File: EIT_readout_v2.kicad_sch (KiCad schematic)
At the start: 16 parts, among them J4 Conn_Coaxial_Small, J5 Conn_Coaxial_Small, J6 Conn_Coaxial_Small, U1 Teensy4.0, U2 MAX336CWI+, U3 MAX336CWI+, U4 LTC1983ES6-3-TRPBF

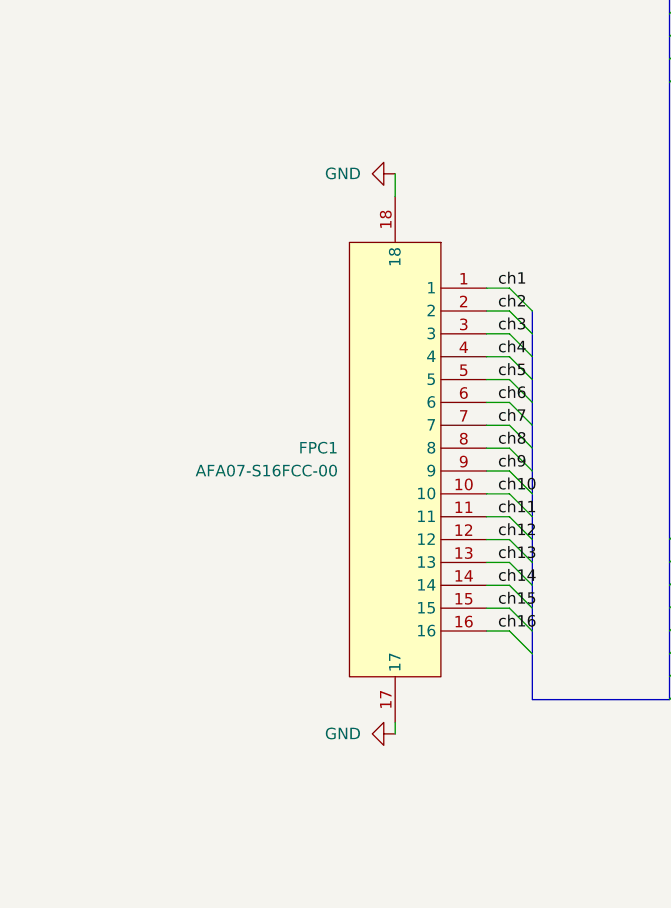
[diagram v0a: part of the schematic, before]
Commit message: changed the readout PCB FPC holder to 18 pins to accommodate ground
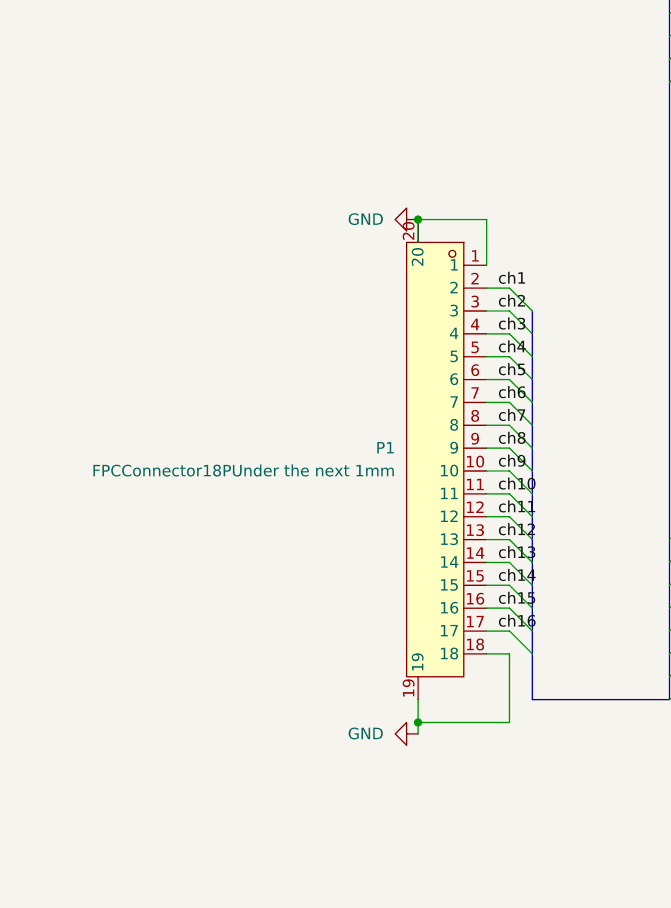
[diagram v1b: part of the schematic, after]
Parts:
- removed FPC1: AFA07-S16FCC-00, easyeda2kicad:FPC-SMD_16P-P1.00_AFA07-S16FCC-00, symbol easyeda2kicad:AFA07-S16FCC-00
- added P1: FPCConnector18PUnder the next 1mm, easyeda2kicad:FPC-SMD_18P-P1.00_AFA07-S18FCC-00, symbol easyeda2kicad:FPCConnector18PUnderthenext1mm
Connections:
- net GND: now also P1.1, P1.18, P1.19, P1.20
- net ch1: now also P1.2
- net ch10: now also P1.11
- net ch11: now also P1.12
- net ch12: now also P1.13
- net ch13: now also P1.14
- net ch14: now also P1.15
- net ch15: now also P1.16
- net ch16: now also P1.17
- net ch2: now also P1.3
- net ch3: now also P1.4
- net ch4: now also P1.5
- net ch5: now also P1.6
- net ch6: now also P1.7
- net ch7: now also P1.8
- net ch8: now also P1.9
- net ch9: now also P1.10
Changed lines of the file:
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@@
 		(color 0 0 0 0)
 	)
+	(junction
+		(at 45.72 139.7)
+		(diameter 0)
+		(color 0 0 0 0)
+	)
+	(junction
+		(at 45.72 83.82)
+		(diameter 0)
+		(color 0 0 0 0)
+	)
 	(no_connect
 		(at 198.12 45.72)
@@
 	(wire
 		(pts
-			(xy 43.18 78.74) (xy 43.18 81.28)
+			(xy 45.72 83.82) (xy 45.72 86.36)
 		)
 		(stroke
@@
 	(wire
 		(pts
+			(xy 55.88 132.08) (xy 55.88 139.7)
+		)
+		(stroke
+			(width 0)
+			(type default)
+		)
+	)
+	(wire
+		(pts
 			(xy 193.04 142.24) (xy 204.47 142.24)
 		)
@@
 	(wire
 		(pts
+			(xy 53.34 83.82) (xy 45.72 83.82)
+		)
+		(stroke
+			(width 0)
+			(type default)
+		)
+	)
+	(wire
+		(pts
 			(xy 85.09 95.25) (xy 85.09 97.79)
 		)
@@
 	(wire
 		(pts
+			(xy 53.34 132.08) (xy 55.88 132.08)
+		)
+		(stroke
+			(width 0)
+			(type default)
+		)
+	)
+	(wire
+		(pts
 			(xy 76.2 129.54) (xy 86.36 129.54)
 		)
@@
 	(wire
 		(pts
-			(xy 43.18 139.7) (xy 43.18 140.97)
+			(xy 45.72 139.7) (xy 45.72 140.97)
 		)
 		(stroke
@@
 	(wire
 		(pts
+			(xy 53.34 88.9) (xy 53.34 83.82)
+		)
+		(stroke
+			(width 0)
+			(type default)
+		)
+	)
+	(wire
+		(pts
 			(xy 53.34 129.54) (xy 55.88 129.54)
 		)
@@
 	(wire
 		(pts
+			(xy 55.88 139.7) (xy 45.72 139.7)
+		)
+		(stroke
+			(width 0)
+			(type default)
+		)
+	)
+	(wire
+		(pts
 			(xy 76.2 53.34) (xy 86.36 53.34)
 		)
@@
 		)
 	)
+	(wire
+		(pts
+			(xy 45.72 137.16) (xy 45.72 139.7)
+		)
+		(stroke
+			(width 0)
+			(type default)
+		)
+	)
 	(bus
 		(pts
@@
 	(symbol
 		(lib_id "power:GND")
-		(at 43.18 78.74 270)
+		(at 45.72 83.82 270)
 		(unit 1)
 		(exclude_from_sim no)
@@
 		(fields_autoplaced yes)
 		(property "Reference" "#PWR020"
-			(at 36.83 78.74 0)
+			(at 39.37 83.82 0)
 			(effects
 				(font
@@
 		)
 		(property "Value" "GND"
-			(at 39.37 78.7399 90)
+			(at 41.91 83.8199 90)
 			(effects
 				(font
@@
 		)
 		(property "Footprint" ""
-			(at 43.18 78.74 0)
+			(at 45.72 83.82 0)
 			(effects
 				(font
@@
 		)
 		(property "Datasheet" ""
-			(at 43.18 78.74 0)
+			(at 45.72 83.82 0)
 			(effects
 				(font
@@
 		)
 		(property "Description" "Power symbol creates a global label with name \"GND\" , ground"
-			(at 43.18 78.74 0)
+			(at 45.72 83.82 0)
 			(effects
 				(font
@@
 	)
 	(symbol
+		(lib_id "easyeda2kicad:FPCConnector18PUnderthenext1mm")
+		(at 49.53 110.49 0)
+		(mirror y)
+		(unit 1)
+		(exclude_from_sim no)
+		(in_bom yes)
+		(on_board yes)
+		(dnp no)
+		(property "Reference" "P1"
+			(at 43.18 109.2199 0)
+			(effects
+				(font
+					(size 1.27 1.27)
+				)
+				(justify left)
+			)
+		)
+		(property "Value" "FPCConnector18PUnder the next 1mm"
+			(at 43.18 111.7599 0)
+			(effects
+				(font
+					(size 1.27 1.27)
+				)
+				(justify left)
+			)
+		)
+		(property "Footprint" "easyeda2kicad:FPC-SMD_18P-P1.00_AFA07-S18FCC-00"
+			(at 49.53 144.78 0)
+			(effects
+				(font
+					(size 1.27 1.27)
+				)
+				(hide yes)
+			)
+		)
+		(property "Datasheet" "https://lcsc.com/product-detail/FPC-Connectors_FPC-1-0mmpitch-18P-Pull-type-Under-the-next_C23826.html"
+			(at 49.53 147.32 0)
+			(effects
+				(font
+					(size 1.27 1.27)
+				)
+				(hide yes)
+			)
+		)
+		(property "Description" "FPC 1.0mm 18P"
+			(at 49.53 110.49 0)
+			(effects
+				(font
+					(size 1.27 1.27)
+				)
+				(hide yes)
+			)
+		)
+		(property "Manufacturer" "JS(钜硕电子)"
+			(at 49.53 149.86 0)
+			(effects
+				(font
+					(size 1.27 1.27)
+				)
+				(hide yes)
+			)
+		)
+		(property "MPN" "AFA07-S18FCC-00"
+			(at 49.53 152.4 0)
+			(effects
+				(font
+					(size 1.27 1.27)
+				)
+				(hide yes)
+			)
+		)
+		(property "LCSC Part" "C23826"
+			(at 49.53 154.94 0)
+			(effects
+				(font
+					(size 1.27 1.27)
+				)
+				(hide yes)
+			)
+		)
+		(pin "7"
+		)
+		(pin "4"
+		)
+		(pin "13"
+		)
+		(pin "2"
+		)
+		(pin "5"
+		)
+		(pin "16"
+		)
+		(pin "20"
+		)
+		(pin "3"
+		)
+		(pin "6"
+		)
+		(pin "9"
+		)
+		(pin "10"
+		)
+		(pin "15"
+		)
+		(pin "11"
+		)
+		(pin "19"
+		)
+		(pin "18"
+		)
+		(pin "1"
+		)
+		(pin "8"
+		)
+		(pin "14"
+		)
+		(pin "17"
+		)
+		(pin "12"
+		)
+		(instances
+			(project ""
+				(path "/e5542335-9a9c-475b-927f-3f88279fb344"
+					(reference "P1")
+					(unit 1)
+				)
+			)
+		)
+	)
+	(symbol
 		(lib_id "power:GND")
 		(at 278.13 85.09 180)
@@
 	(symbol
 		(lib_id "power:GND")
-		(at 43.18 140.97 270)
+		(at 45.72 140.97 270)
 		(unit 1)
 		(exclude_from_sim no)
@@
 		(fields_autoplaced yes)
 		(property "Reference" "#PWR021"
-			(at 36.83 140.97 0)
+			(at 39.37 140.97 0)
 			(effects
 				(font
@@
 		)
 		(property "Value" "GND"
-			(at 39.37 140.9699 90)
+			(at 41.91 140.9699 90)
 			(effects
 				(font
@@
 		)
 		(property "Footprint" ""
-			(at 43.18 140.97 0)
+			(at 45.72 140.97 0)
 			(effects
 				(font
@@
 		)
 		(property "Datasheet" ""
-			(at 43.18 140.97 0)
+			(at 45.72 140.97 0)
 			(effects
 				(font
@@
 		)
 		(property "Description" "Power symbol creates a global label with name \"GND\" , ground"
-			(at 43.18 140.97 0)
+			(at 45.72 140.97 0)
 			(effects
 				(font
@@
 					(unit 1)
 				)
-			)
-		)
-	)
-	(symbol
-		(lib_id "easyeda2kicad:AFA07-S16FCC-00")
-		(at 45.72 110.49 270)
-		(unit 1)
-		(exclude_from_sim no)
-		(in_bom yes)
-		(on_board yes)
-		(dnp no)
-		(fields_autoplaced yes)
-		(property "Reference" "FPC1"
-			(at 36.83 109.2199 90)
-			(effects
-				(font
-					(size 1.27 1.27)
-				)
-				(justify right)
-			)
-		)
-		(property "Value" "AFA07-S16FCC-00"
-			(at 36.83 111.7599 90)
-			(effects
-				(font
-					(size 1.27 1.27)
-				)
-				(justify right)
-			)
-		)
-		(property "Footprint" "easyeda2kicad:FPC-SMD_16P-P1.00_AFA07-S16FCC-00"
-			(at 35.56 110.49 0)
-			(effects
-				(font
-					(size 1.27 1.27)
-				)
-				(hide yes)
-			)
-		)
-		(property "Datasheet" "https://lcsc.com/product-detail/FPC-Connectors_Made-in-China-FPC-1-0mmpitch-16P-Pull-type_C13744.html"
-			(at 33.02 110.49 0)
-			(effects
-				(font
-					(size 1.27 1.27)
-				)
-				(hide yes)
-			)
-		)
-		(property "Description" ""
-			(at 45.72 110.49 0)
-			(effects
-				(font
-					(size 1.27 1.27)
-				)
-				(hide yes)
-			)
-		)
-		(property "Manufacturer" "JS(钜硕电子)"
-			(at 30.48 110.49 0)
-			(effects
-				(font
-					(size 1.27 1.27)
-				)
-				(hide yes)
-			)
-		)
-		(property "MPN" "AFA07-S16FCC-00"
-			(at 27.94 110.49 0)
-			(effects
-				(font
-					(size 1.27 1.27)
-				)
-				(hide yes)
-			)
-		)
-		(property "LCSC Part" "C13744"
-			(at 25.4 110.49 0)
-			(effects
-				(font
-					(size 1.27 1.27)
-				)
-				(hide yes)
-			)
-		)
-		(pin "18"
-		)
-		(pin "1"
-		)
-		(pin "3"
-		)
-		(pin "4"
-		)
-		(pin "8"
-		)
-		(pin "2"
-		)
-		(pin "15"
-		)
-		(pin "11"
-		)
-		(pin "16"
-		)
-		(pin "14"
-		)
-		(pin "10"
-		)
-		(pin "9"
-		)
-		(pin "13"
-		)
-		(pin "5"
-		)
-		(pin "7"
-		)
-		(pin "17"
-		)
-		(pin "6"
-		)
-		(pin "12"
-		)
-		(instances
-			(project ""
-				(path "/e5542335-9a9c-475b-927f-3f88279fb344"
-					(reference "FPC1")
-					(unit 1)
-				)
